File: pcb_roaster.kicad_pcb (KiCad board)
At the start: 2 copper layers, 67.3 x 67.3 mm, 39 parts, among them J1 Screw_Terminal_01x02, J2 Screw_Terminal_01x02, J3 Screw_Terminal_01x03, SW1 SW_Push, U1 MAX31855KASA, U2 MAX31855KASA

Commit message: Update PCB
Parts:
- A1: footprint Module:Adafruit_Feather_WithMountingHoles -> Module:Adafruit_Feather
- C1, C2: value 10u -> 100n

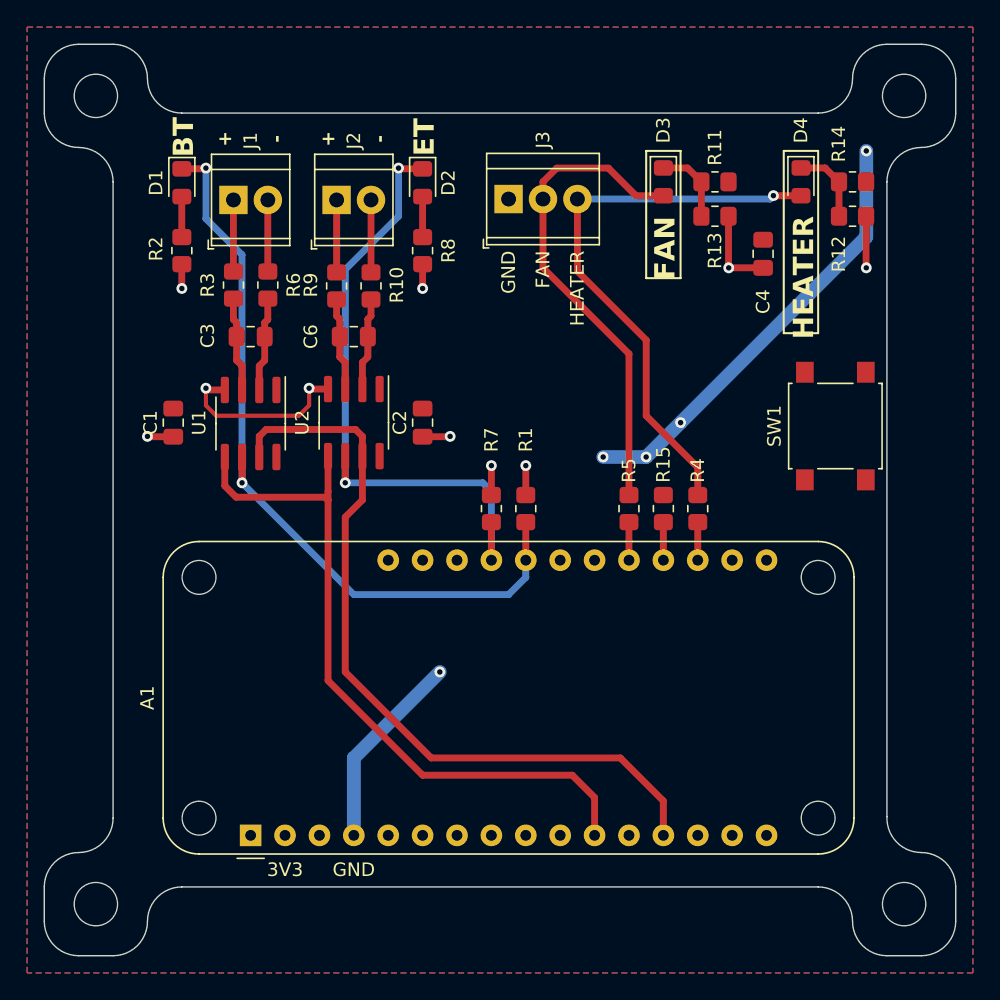
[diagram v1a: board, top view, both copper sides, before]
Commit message: Clear DRC issues
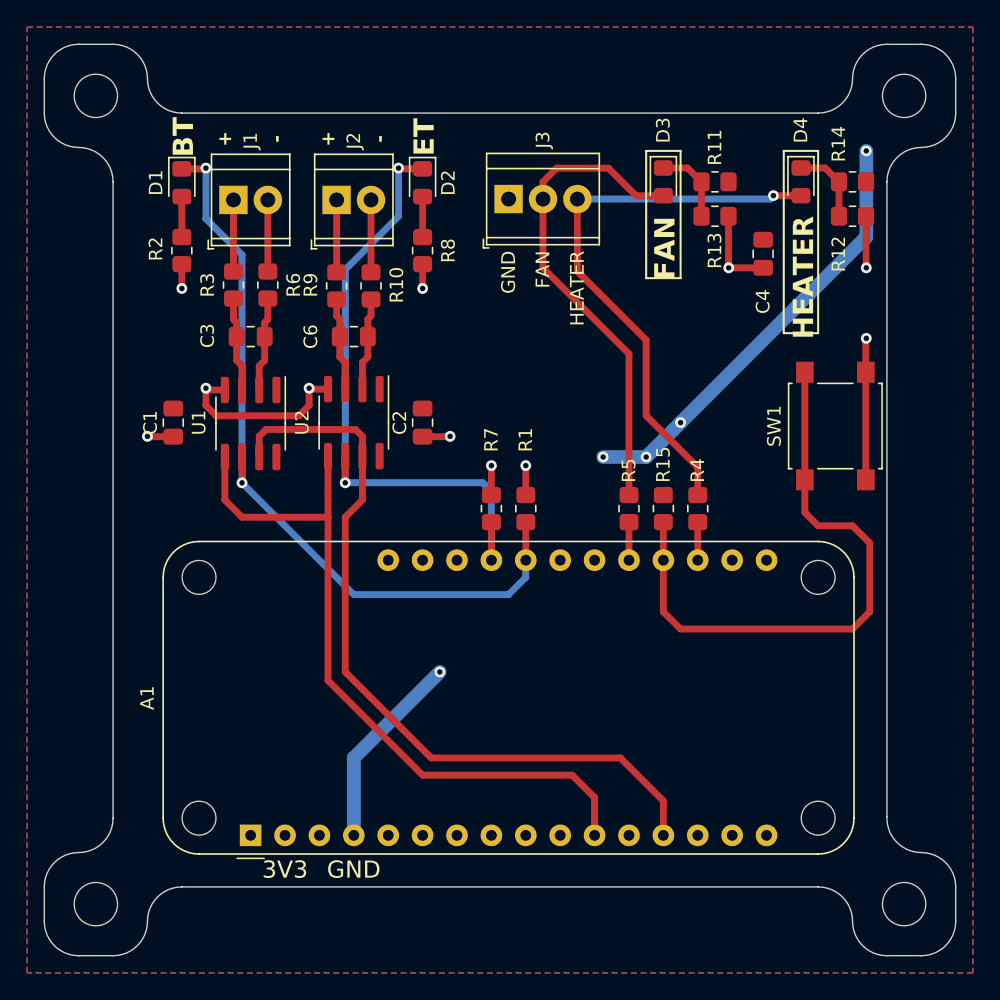
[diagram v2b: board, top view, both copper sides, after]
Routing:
- net /button: track 2.81 -> 44.1 mm
- net +3V3: track 35.7 -> 46.2 mm, vias 10 -> 11
- net /sck: track 52.7 -> 53.8 mm
